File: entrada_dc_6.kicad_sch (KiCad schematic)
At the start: 4 parts

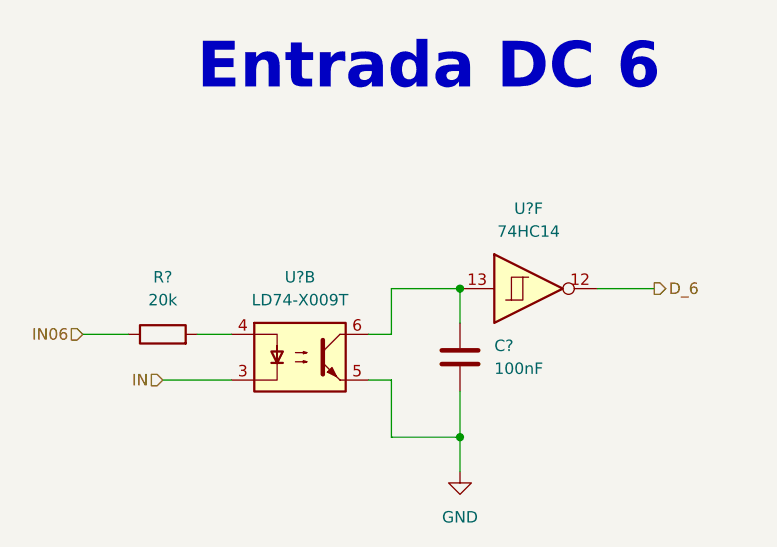
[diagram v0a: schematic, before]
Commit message: input/output separadas
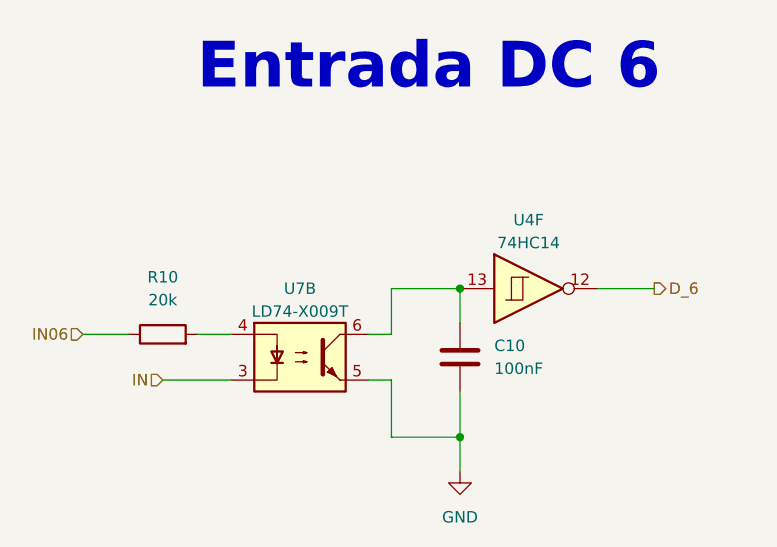
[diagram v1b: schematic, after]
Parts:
- gave numbers to parts that had none: 4
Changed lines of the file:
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@@
 (kicad_sch (version 20221004) (generator eeschema)
   (paper "A4" portrait)
+  (title_block
+    (date "2022-10-09")
+    (rev "José Luis Laica")
+  )
   (junction (at 114.3 125.73) (diameter 0) (color 0 0 0 0)
   )
@@
   (symbol (lib_id "Device:R") (at 81.28 114.3 90) (unit 1)
     (in_bom yes) (on_board yes) (dnp no) (fields_autoplaced)
-    (property "Reference" "R?" (at 81.28 107.95 90)
+    (property "Reference" "R10" (at 81.28 107.95 90)
       (effects (font (size 1.27 1.27)))
     )
@@
       (project "PLC 32 V2"
         (path "/d17a54f1-6eda-453f-95e1-42a53b02a1c3/3c7a123d-7923-42e8-abad-a742ed3daa97"
-          (reference "R?") (unit 1) (value "20k") (footprint "Resistor_SMD:R_0603_1608Metric")
+          (reference "R10") (unit 1) (value "20k") (footprint "Resistor_SMD:R_0603_1608Metric")
         )
       )
@@
   (symbol (lib_id "power:GND") (at 114.3 129.54 0) (unit 1)
     (in_bom yes) (on_board yes) (dnp no) (fields_autoplaced)
-    (property "Reference" "#PWR?" (at 114.3 135.89 0)
+    (property "Reference" "#PWR011" (at 114.3 135.89 0)
       (effects (font (size 1.27 1.27)) hide)
     )
@@
       (project "PLC 32 V2"
         (path "/d17a54f1-6eda-453f-95e1-42a53b02a1c3/3c7a123d-7923-42e8-abad-a742ed3daa97"
-          (reference "#PWR?") (unit 1) (value "GND") (footprint "")
+          (reference "#PWR011") (unit 1) (value "GND") (footprint "")
         )
       )
@@
   (symbol (lib_id "Device:C") (at 114.3 116.84 0) (unit 1)
     (in_bom yes) (on_board yes) (dnp no) (fields_autoplaced)
-    (property "Reference" "C?" (at 118.11 115.5699 0)
+    (property "Reference" "C10" (at 118.11 115.5699 0)
       (effects (font (size 1.27 1.27)) (justify left))
     )
@@
       (project "PLC 32 V2"
         (path "/d17a54f1-6eda-453f-95e1-42a53b02a1c3/3c7a123d-7923-42e8-abad-a742ed3daa97"
-          (reference "C?") (unit 1) (value "100nF") (footprint "Capacitor_SMD:C_0402_1005Metric")
+          (reference "C10") (unit 1) (value "100nF") (footprint "Capacitor_SMD:C_0402_1005Metric")
         )
       )
@@
   (symbol (lib_id "74xx:74HC14") (at 121.92 109.22 0) (unit 6)
     (in_bom yes) (on_board yes) (dnp no) (fields_autoplaced)
-    (property "Reference" "U?" (at 121.92 100.33 0)
+    (property "Reference" "U4" (at 121.92 101.6 0)
       (effects (font (size 1.27 1.27)))
     )
-    (property "Value" "74HC14" (at 121.92 102.87 0)
+    (property "Value" "74HC14" (at 121.92 104.14 0)
       (effects (font (size 1.27 1.27)))
     )
@@
       (project "PLC 32 V2"
         (path "/d17a54f1-6eda-453f-95e1-42a53b02a1c3/3c7a123d-7923-42e8-abad-a742ed3daa97"
-          (reference "U?") (unit 6) (value "74HC14") (footprint "Package_SO:SOIC-14W_7.5x9mm_P1.27mm")
+          (reference "U4") (unit 6) (value "74HC14") (footprint "Package_SO:SOIC-14W_7.5x9mm_P1.27mm")
         )
       )
@@
   (symbol (lib_id "Isolator:ILD74") (at 96.52 116.84 0) (unit 2)
     (in_bom yes) (on_board yes) (dnp no) (fields_autoplaced)
-    (property "Reference" "U?" (at 96.52 107.95 0)
+    (property "Reference" "U7" (at 96.52 109.22 0)
       (effects (font (size 1.27 1.27)))
     )
-    (property "Value" "LD74-X009T" (at 96.52 110.49 0)
+    (property "Value" "LD74-X009T" (at 96.52 111.76 0)
       (effects (font (size 1.27 1.27)))
     )
@@
       (project "PLC 32 V2"
         (path "/d17a54f1-6eda-453f-95e1-42a53b02a1c3/3c7a123d-7923-42e8-abad-a742ed3daa97"
-          (reference "U?") (unit 2) (value "LD74-X009T") (footprint "Package_DIP:DIP-8_W8.89mm_SMDSocket_LongPads")
+          (reference "U7") (unit 2) (value "LD74-X009T") (footprint "Package_DIP:DIP-8_W8.89mm_SMDSocket_LongPads")
         )
       )

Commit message: add
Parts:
- renumbered C10 to C11, R10 to R40, U7 to U10, U4 to U7
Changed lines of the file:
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@@
   (symbol (lib_id "Device:R") (at 81.28 114.3 90) (unit 1)
     (in_bom yes) (on_board yes) (dnp no) (fields_autoplaced)
-    (property "Reference" "R10" (at 81.28 107.95 90)
+    (property "Reference" "R40" (at 81.28 107.95 90)
       (effects (font (size 1.27 1.27)))
     )
@@
       (project "PLC 32 V2"
         (path "/d17a54f1-6eda-453f-95e1-42a53b02a1c3/3c7a123d-7923-42e8-abad-a742ed3daa97"
-          (reference "R10") (unit 1) (value "20k") (footprint "Resistor_SMD:R_0603_1608Metric")
+          (reference "R40") (unit 1) (value "20k") (footprint "Resistor_SMD:R_0603_1608Metric")
         )
       )
@@
   (symbol (lib_id "Device:C") (at 114.3 116.84 0) (unit 1)
     (in_bom yes) (on_board yes) (dnp no) (fields_autoplaced)
-    (property "Reference" "C10" (at 118.11 115.5699 0)
+    (property "Reference" "C11" (at 118.11 115.5699 0)
       (effects (font (size 1.27 1.27)) (justify left))
     )
@@
       (project "PLC 32 V2"
         (path "/d17a54f1-6eda-453f-95e1-42a53b02a1c3/3c7a123d-7923-42e8-abad-a742ed3daa97"
-          (reference "C10") (unit 1) (value "100nF") (footprint "Capacitor_SMD:C_0402_1005Metric")
+          (reference "C11") (unit 1) (value "100nF") (footprint "Capacitor_SMD:C_0402_1005Metric")
         )
       )
@@
   (symbol (lib_id "74xx:74HC14") (at 121.92 109.22 0) (unit 6)
     (in_bom yes) (on_board yes) (dnp no) (fields_autoplaced)
-    (property "Reference" "U4" (at 121.92 101.6 0)
+    (property "Reference" "U7" (at 121.92 101.6 0)
       (effects (font (size 1.27 1.27)))
     )
@@
       (project "PLC 32 V2"
         (path "/d17a54f1-6eda-453f-95e1-42a53b02a1c3/3c7a123d-7923-42e8-abad-a742ed3daa97"
-          (reference "U4") (unit 6) (value "74HC14") (footprint "Package_SO:SOIC-14W_7.5x9mm_P1.27mm")
+          (reference "U7") (unit 6) (value "74HC14") (footprint "Package_SO:SOIC-14W_7.5x9mm_P1.27mm")
         )
       )
@@
   (symbol (lib_id "Isolator:ILD74") (at 96.52 116.84 0) (unit 2)
     (in_bom yes) (on_board yes) (dnp no) (fields_autoplaced)
-    (property "Reference" "U7" (at 96.52 109.22 0)
+    (property "Reference" "U10" (at 96.52 109.22 0)
       (effects (font (size 1.27 1.27)))
     )
@@
       (project "PLC 32 V2"
         (path "/d17a54f1-6eda-453f-95e1-42a53b02a1c3/3c7a123d-7923-42e8-abad-a742ed3daa97"
-          (reference "U7") (unit 2) (value "LD74-X009T") (footprint "Package_DIP:DIP-8_W8.89mm_SMDSocket_LongPads")
+          (reference "U10") (unit 2) (value "LD74-X009T") (footprint "Package_DIP:DIP-8_W8.89mm_SMDSocket_LongPads")
         )
       )
